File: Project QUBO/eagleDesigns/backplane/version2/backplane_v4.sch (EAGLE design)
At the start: 206 parts, among them IC1 MC78M08ABDTG, U1 TUSB2077ALQFP

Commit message: 
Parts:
- removed C12, C14, C15: 100n, resistor:C-USC0805
- removed C13: 4.7u, resistor:C-USC0805
- removed C21, C22, C23, C24, C25: (no value), resistor:C-USC0805
- removed IC1: MC78M08ABDTG, linear:MC78M08ABDTG
- removed IMU_FTDI: FT232RQ, ftdichip:FT232RQ
- removed IMU_TTL-TO-RS422: AD7306JRZ, analog_devices:AD7306JRZ
- removed LED5, LED6: (no value), led:LEDCHIPLED_0805
- added 2PIN_4: Magnetic Reed Switch plug, molex:KK254_VERT_2PIN22-29-2021
- added D1: Vz=14V, diode:ZENER-DIODESOD123
- added R62, R63: 5k, resistor:R-US_R0805
- added U$42, U$52, U$53, U$54, U$55, U$56, U$57, U$58, U$59, U$60, U$61, U$62, U$63: PRTR5V0U2X, NXP:PRTR5V0U2X
- added U$43: AHRS USB header, connectors:USB_4PIN_VERT
- added U$44, U$48: (no value), littelfuse:V5.5MLA0805
- added U$45, U$49, U$51: 100u_tant, avx:F93-XX-XXX-X-A
- added U$46: I2C level shifter, texas:PCA9306DCT
- added U$47: Depth Sensor header, connectors:DF13-4
- added U$50: P82B715, NXP:P82B715
- R1: value 120 -> 200k
- R61: value 15k -> 50k
- R8, R9: value 270 -> 5k
- U$10: value (none) -> IMU USB header; device hirose:HR30-6R-6PD -> connectors:USB_4PIN_VERT
- U$11: value 1U_tant -> (none); device avx:F93-XX-XXX-X-A -> littelfuse:V5.5MLA0805
- U$12: value 1U_tant -> 100u_tant
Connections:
- removed net 8V: IC1.VO, U$10.2, U$12.+
- removed net IMU_RX: IMU_FTDI.RXD, IMU_TTL-TO-RS422.R1-OUT
- removed net IMU_RXD_M: IMU_TTL-TO-RS422.R1-IN(B), R1.1, U$10.4, U$9.I/O_2
- removed net IMU_RXD_P: IMU_TTL-TO-RS422.R1-IN/(A), R1.2, U$10.3, U$9.I/O_1
- removed net N$26: C12.1, IMU_FTDI.3V3OUT
- removed net N$27: IMU_FTDI.CBUS1, LED6.C
- removed net N$28: IMU_FTDI.CBUS0, LED5.C
- removed net N$29: LED5.A, R8.1
- removed net N$30: LED6.A, R9.1
- removed net N$37: C21.1, IMU_TTL-TO-RS422.V+
- removed net N$38: C22.1, IMU_TTL-TO-RS422.V-
- removed net N$40: C23.2, IMU_TTL-TO-RS422.C1-
- removed net N$41: C24.1, IMU_TTL-TO-RS422.C2+
- removed net N$42: C24.2, IMU_TTL-TO-RS422.C2-
- new net DEPTH_SCL: R62.2, U$46.SCL1, U$47.2
- new net DEPTH_SDA: R63.2, U$46.SDA1, U$47.3
- new net GND1: U$11.P$1, U$12.-
- new net GND2: U$44.P$1, U$45.-
- new net GND3: U$48.P$1, U$49.-
- new net SCL_1_UNBUF: R8.2, U$46.SCL2, U$50.SX
- new net SDA_1_UNBUF: R9.2, U$46.SDA2, U$50.SY
- new net USB_5_5V1: U$11.P$2, U$12.+
- new net USB_5_5V2: U$44.P$2, U$45.+
- new net USB_5_5V3: U$48.P$2, U$49.+
- net 12V: now also 2PIN_4.P$1, U$42.VCC; no longer IC1.VI, U$11.+
- net 3V3: now also R62.1, R63.1, U$46.VREF1
- net 5V: now also R1.2, R8.1, R9.1, U$10.1, U$43.1, U$47.1, U$50.VCC, U$52.VCC, U$53.VCC, U$54.VCC, U$55.VCC, U$56.VCC, U$57.VCC, U$58.VCC, U$59.VCC, U$60.VCC, U$61.VCC, U$62.VCC, U$63.VCC; no longer C13.1, C14.1, C15.1, C25.1, IMU_FTDI.!RESET, IMU_FTDI.VCC, IMU_FTDI.VCCIO, IMU_TTL-TO-RS422.VCC, R8.2, R9.2
- net ACT-PWR_PRE-KILL: now also D1.C
- net AHRS_USB_M: now also U$42.I/O_2, U$43.3
- net AHRS_USB_P: now also U$42.I/O_1, U$43.2
- net BATT1_SCL: now also U$62.I/O_1
- net BATT1_SDA: now also U$62.I/O_2
- net BATT2_SCL: now also U$61.I/O_1
- net BATT2_SDA: now also U$61.I/O_2
- net CANH: now also U$53.I/O_2
- net CANL: now also U$53.I/O_1
- net CTS_5: now also U$55.I/O_2
- net DVL_HCTS: now also U$58.I/O_2
- net DVL_HRTS: now also U$57.I/O_1
- net DVL_HRX: now also U$56.I/O_2
- net DVL_HTX: now also U$57.I/O_2
- net DVL_SCTS: now also U$56.I/O_1
- net DVL_SRTS: now also U$59.I/O_2
- net DVL_SRX: now also U$58.I/O_1
- net DVL_STX: now also U$59.I/O_1
- net GND: now also U$10.4, U$42.GND, U$43.4, U$46.GND, U$47.4, U$50.GND, U$51.-, U$52.GND, U$53.GND, U$54.GND, U$55.GND, U$56.GND, U$57.GND, U$58.GND, U$59.GND, U$60.GND, U$61.GND, U$62.GND, U$63.GND; no longer C12.2, C13.2, C14.2, C15.2, C21.2, C22.2, C25.2, IC1.GND, IMU_FTDI.GND, IMU_FTDI.GND@1, IMU_FTDI.GND@2, IMU_FTDI.GND@A, IMU_FTDI.TEST, IMU_TTL-TO-RS422.232/!422!, IMU_TTL-TO-RS422.GND@14, IMU_TTL-TO-RS422.GND@18, U$10.5, U$11.-, U$12.-
- net IMU_USB_M: now also U$10.3, U$9.I/O_2; no longer IMU_FTDI.USBDM
- net IMU_USB_P: now also U$10.2, U$9.I/O_1; no longer IMU_FTDI.USBDP
- net N$39: now also R1.1, U$46.EN, U$46.VREF2, U$51.+; no longer C23.1, IMU_TTL-TO-RS422.C1+
- net N$73: now also 2PIN_4.P$2, D1.A
- net RTS_5: now also U$55.I/O_1
- net RX_5: now also U$54.I/O_1
- net SCL_1: now also U$50.LX
- net SCL_2: now also U$63.I/O_1
- net SCL_3: now also U$52.I/O_1
- net SDA_1: now also U$50.LY
- net SDA_2: now also U$63.I/O_2
- net SDA_3: now also U$52.I/O_2
- net SHORE_SCL: now also U$60.I/O_1
- net SHORE_SDA: now also U$60.I/O_2
- net TX_5: now also U$54.I/O_2
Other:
- note added: "AHRS Connection"
- note added: "DVL USB-UART Converters"
- note added: "Depth Sensor Connection"
- note removed: "USB-UART Converters"
- moved on the sheet: R1, R8, R9, U$12

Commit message: 
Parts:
- added D10, D11, D12, D13, D14, D15, D16, D17, D18, D19, D2, D20, D21, D22, D23, D24, D25, D26, D27, D28, D29, D3, D30, D31, D32, D33, D34, D35, D4, D5, D6, D7, D8, D9: (no value), diode:ZENER-DIODESOD123
- added U$64, U$65, U$66, U$67, U$70, U$71, U$72, U$73, U$74, U$75, U$76, U$77, U$78, U$79, U$80, U$81, U$82, U$83, U$84, U$85, U$86, U$87, U$88, U$89, U$90, U$91, U$92, U$93, U$94, U$95, U$96, U$97, U$98, U$99: 0.1u, avx:F93-XX-XXX-X-A
- added U$68: (no value), littelfuse:V5.5MLA0805
- added U$69: 100u_tant, avx:F93-XX-XXX-X-A
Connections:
- removed net N$73: 2PIN_4.P$2, D1.A, R61.1, U$41.P$3
- new net KILL-SWT-GATE: 2PIN_4.P$2, D1.A, D10.C, R61.1, U$41.P$3, U$74.+
- net 12V: now also D11.C, D15.C, D19.C, D23.C, D27.C, D4.C, D5.C, D6.C, D7.C, U$64.+, U$65.+, U$66.+, U$67.+, U$75.+, U$79.+, U$83.+, U$87.+, U$91.+
- net 3V3: now also D13.C, D17.C, D21.C, D25.C, U$77.+, U$81.+, U$85.+, U$89.+
- net 5V: now also D12.C, D16.C, D2.C, D20.C, D24.C, D3.C, U$68.P$2, U$69.+, U$70.+, U$71.+, U$76.+, U$80.+, U$84.+, U$88.+
- net ACT-PWR_POST-KILL: now also D8.C, U$72.+
- net ACT-PWR_PRE-KILL: now also D9.C, U$73.+
- net GND: now also D10.A, D11.A, D12.A, D13.A, D14.A, D15.A, D16.A, D17.A, D18.A, D19.A, D2.A, D20.A, D21.A, D22.A, D23.A, D24.A, D25.A, D26.A, D27.A, D28.A, D29.A, D3.A, D30.A, D31.A, D32.A, D33.A, D34.A, D35.A, D4.A, D5.A, D6.A, D7.A, D8.A, D9.A, U$64.-, U$65.-, U$66.-, U$67.-, U$68.P$1, U$69.-, U$70.-, U$71.-, U$72.-, U$73.-, U$74.-, U$75.-, U$76.-, U$77.-, U$78.-, U$79.-, U$80.-, U$81.-, U$82.-, U$83.-, U$84.-, U$85.-, U$86.-, U$87.-, U$88.-, U$89.-, U$90.-, U$91.-, U$92.-, U$93.-, U$94.-, U$95.-, U$96.-, U$97.-, U$98.-, U$99.-
- net V_BATT: now also D14.C, D18.C, D22.C, D26.C, D28.C, D29.C, D30.C, D31.C, D32.C, D33.C, D34.C, D35.C, U$78.+, U$82.+, U$86.+, U$90.+, U$92.+, U$93.+, U$94.+, U$95.+, U$96.+, U$97.+, U$98.+, U$99.+
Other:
- note added: "Power Line Protections"
- moved on the sheet: SYS-GND_0, SYS-GND_1, SYS-GND_2, SYS-GND_3

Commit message: 
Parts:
- removed SYS-GND_0, SYS-GND_1, SYS-GND_2, SYS-GND_3: SUPERSABRE_2CIRCUIT, molex:SUPERSABRE_2CIRCUIT
- removed U$17: (no value), connectors:USB_4PIN_VERT
- removed U$21: PRTR5V0U2X, NXP:PRTR5V0U2X
- removed U$26: (no value), littelfuse:V5.5MLA0805
- removed U$36: 100u_tant, avx:F93-XX-XXX-X-A
- removed U$74: 0.1u, avx:F93-XX-XXX-X-A
- added D36, D37, D39, D40, D41: 5V, diode:ZENER-DIODESOD123
- added R64, R65, R66: 15k, resistor:R-US_R0805
- added U$100: SYSTEM GROUND, molex:SUPERSABRE_8CIRCUIT
- C26: value 0.1u\ -> 0.1u
- C27, C29: value (none) -> 0.1u
- D1: value Vz=14V -> 14V
- D10, D12, D16, D2, D20, D24, D3: value (none) -> 5V
- D11, D15, D19, D23, D27, D4, D5, D6, D7: value (none) -> 12V
- D13, D17, D21, D25: value (none) -> 3V3
- D14, D18, D22, D26, D28, D29, D30, D31, D32, D33, D34, D35, D8, D9: value (none) -> V_BATT
- LED1, LED3: value (none) -> Red
- LED2, LED4, LED7: value (none) -> Green
- U$64, U$65, U$66, U$67, U$70, U$71, U$72, U$73, U$75, U$76, U$77, U$78, U$79, U$80, U$81, U$82, U$83, U$84, U$85, U$86, U$87, U$88, U$89, U$90, U$91, U$92, U$93, U$94, U$95, U$96, U$97, U$98, U$99: value 0.1u -> 0.1u_tant
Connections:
- net !USB_7_PWR! renamed !EXT_USB_PWR!
- removed net !USB_7_OVERCUR!: G1.!OC3!, U1.!OVERCUR7!
- removed net USB_7_5V: G1.OUT3, U$17.1, U$26.P$2, U$36.+
- removed net USB_7_M: R34.2, R47.1, U$17.3, U$21.I/O_2
- removed net USB_7_P: R35.2, R48.1, U$17.2, U$21.I/O_1
- new net !EXT_USB_OVERCUR!: G1.!OC3!, R66.1, U1.!OVERCUR7!
- new net EXT_USB_5V: 5.7.P$4, D41.C, G1.OUT3, U$68.P$2, U$69.+
- net !USB_5_OVERCUR!: now also R64.2
- net !USB_6_OVERCUR!: now also R65.1
- net 3V3: now also R64.1, R65.2, R66.2
- net 5V: no longer 5.7.P$4, U$21.VCC, U$68.P$2, U$69.+
- net EXT_USB_M: now also R34.2, R47.1
- net EXT_USB_P: now also R35.2, R48.1
- net GND: now also D39.A, D40.A, D41.A, U$100.1, U$100.2, U$100.3, U$100.4, U$100.5, U$100.6, U$100.7, U$100.8; no longer D10.A, SYS-GND_0.P$1, SYS-GND_0.P$2, SYS-GND_1.P$1, SYS-GND_1.P$2, SYS-GND_2.P$1, SYS-GND_2.P$2, SYS-GND_3.P$1, SYS-GND_3.P$2, U$17.4, U$21.GND, U$26.P$1, U$36.-, U$74.-
- net GND1: now also D37.A
- net GND2: now also D36.A
- net GND3: now also D10.A
- net KILL-SWT-GATE: no longer D10.C, U$74.+
- net USB_5_5V: now also D40.C
- net USB_5_5V1: now also D37.C
- net USB_5_5V2: now also D36.C
- net USB_5_5V3: now also D10.C
- net USB_6_5V: now also D39.C
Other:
- moved on the sheet: D10

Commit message: 
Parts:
- G1: value (none) -> TPS2044BBD-SOIC
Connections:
- net 12V: no longer U$42.VCC, U$9.VCC
- net 5V: now also U$42.VCC, U$9.VCC
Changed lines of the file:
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@@
 <text x="-284.48" y="-396.24" size="6.4516" layer="91">IMU Connection</text>
 <text x="-561.34" y="-144.78" size="6.4516" layer="91">Debug LED SPI</text>
-<text x="-530.86" y="-342.9" size="6.4516" layer="91">GPIO USBs</text>
+<text x="-533.4" y="-302.26" size="6.4516" layer="91">GPIO USBs</text>
 <text x="-472.44" y="203.2" size="6.4516" layer="91">7-port USB hub</text>
 <text x="-297.18" y="-142.24" size="6.4516" layer="91">2-port USB hub (DVL)</text>
@@
 <pinref part="D24" gate="G$1" pin="C"/>
 </segment>
+<segment>
+<pinref part="U$9" gate="G$1" pin="VCC"/>
+<wire x1="-266.7" y1="-370.84" x2="-259.08" y2="-370.84" width="0.1524" layer="91"/>
+<label x="-264.16" y="-370.84" size="1.778" layer="95"/>
+</segment>
+<segment>
+<pinref part="U$42" gate="G$1" pin="VCC"/>
+<wire x1="-269.24" y1="-434.34" x2="-261.62" y2="-434.34" width="0.1524" layer="91"/>
+<label x="-266.7" y="-434.34" size="1.778" layer="95"/>
+</segment>
 </net>
 <net name="12V" class="0">
@@
 </segment>
 <segment>
-<pinref part="U$9" gate="G$1" pin="VCC"/>
-<wire x1="-266.7" y1="-370.84" x2="-259.08" y2="-370.84" width="0.1524" layer="91"/>
-<label x="-264.16" y="-370.84" size="1.778" layer="95"/>
-</segment>
-<segment>
-<pinref part="U$42" gate="G$1" pin="VCC"/>
-<wire x1="-269.24" y1="-434.34" x2="-261.62" y2="-434.34" width="0.1524" layer="91"/>
-<label x="-266.7" y="-434.34" size="1.778" layer="95"/>
-</segment>
-<segment>
 <pinref part="2PIN_4" gate="U1" pin="P$1"/>
 <wire x1="398.78" y1="0" x2="393.7" y2="0" width="0.1524" layer="91"/>
@@
 <segment>
 <wire x1="-576.58" y1="-215.9" x2="-439.42" y2="-215.9" width="0.1524" layer="91"/>
-<wire x1="-439.42" y1="-215.9" x2="-439.42" y2="-353.06" width="0.1524" layer="91"/>
-<wire x1="-439.42" y1="-353.06" x2="-576.58" y2="-353.06" width="0.1524" layer="91"/>
-<wire x1="-576.58" y1="-353.06" x2="-576.58" y2="-215.9" width="0.1524" layer="91"/>
+<wire x1="-439.42" y1="-215.9" x2="-439.42" y2="-312.42" width="0.1524" layer="91"/>
+<wire x1="-439.42" y1="-312.42" x2="-576.58" y2="-312.42" width="0.1524" layer="91"/>
+<wire x1="-576.58" y1="-312.42" x2="-576.58" y2="-215.9" width="0.1524" layer="91"/>
 </segment>
 </net>

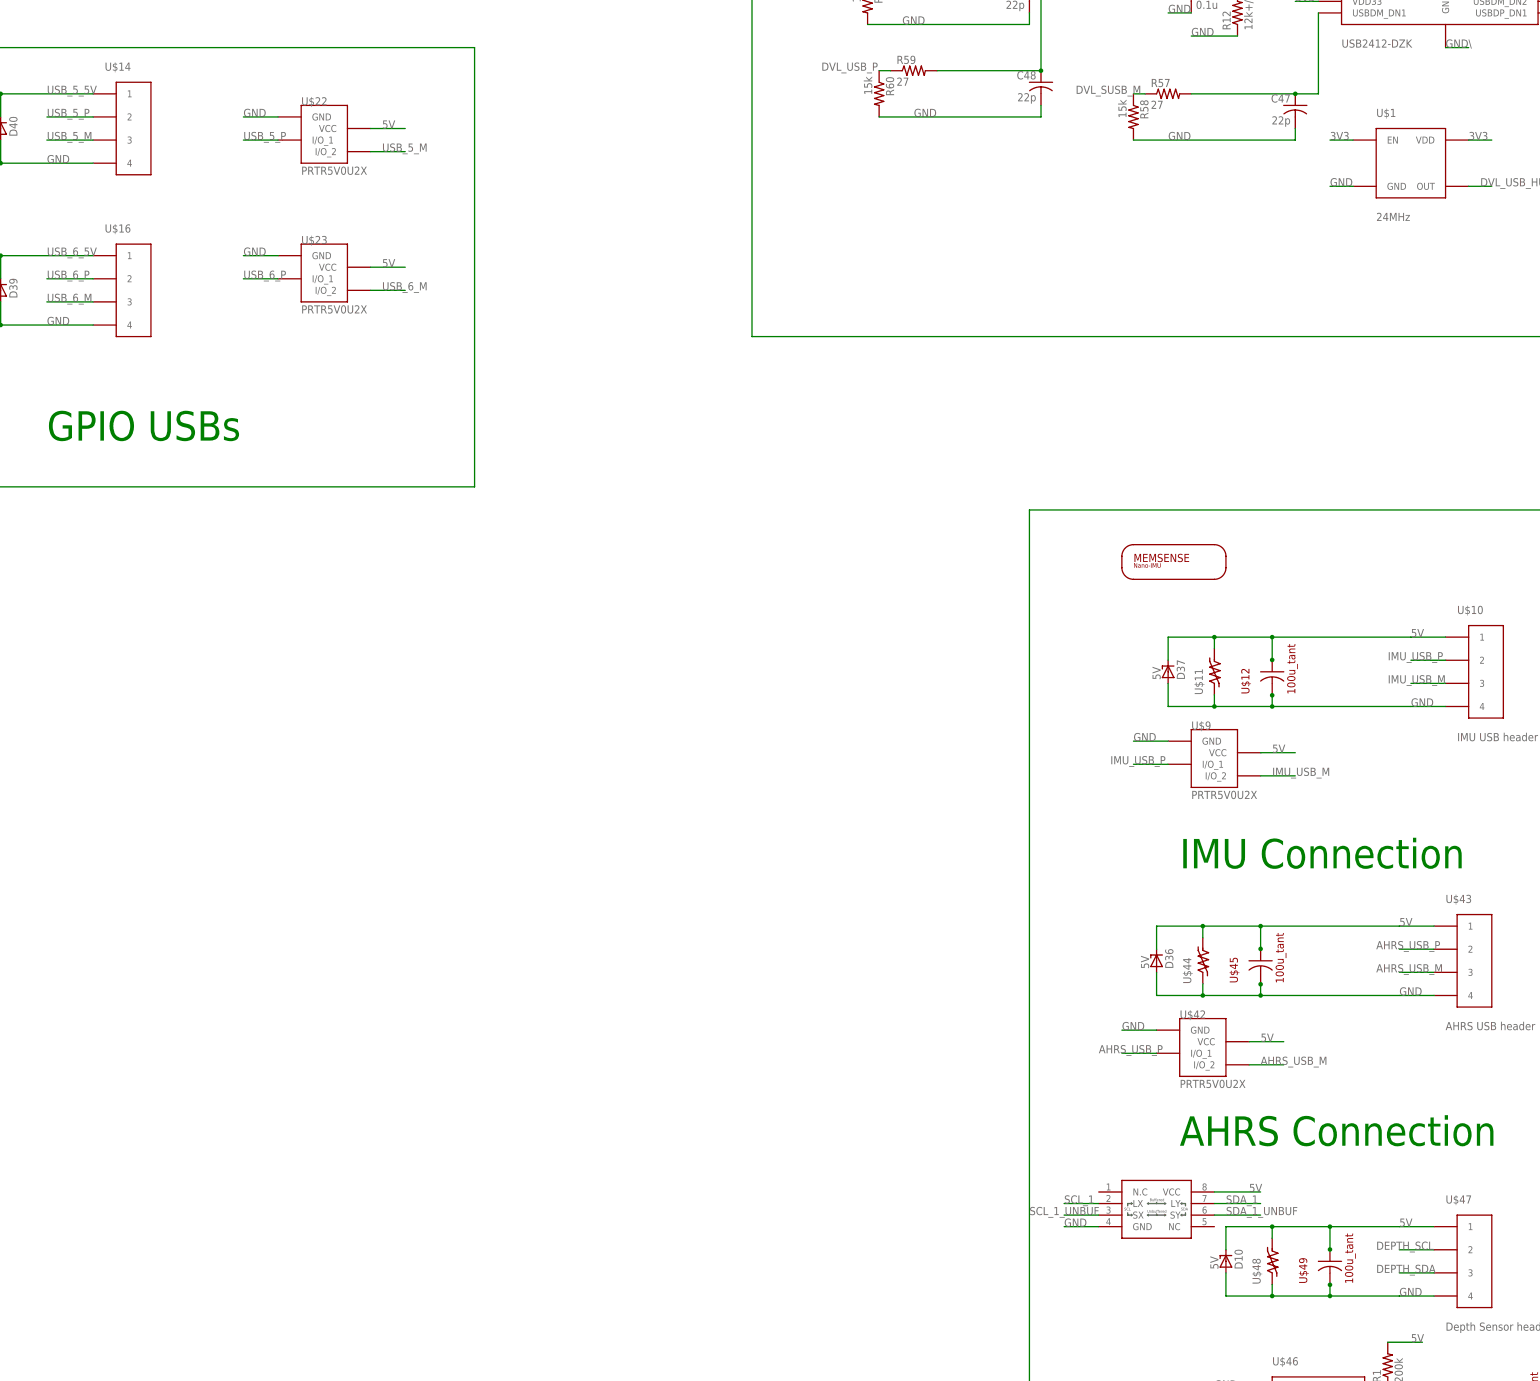
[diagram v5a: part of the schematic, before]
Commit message: 
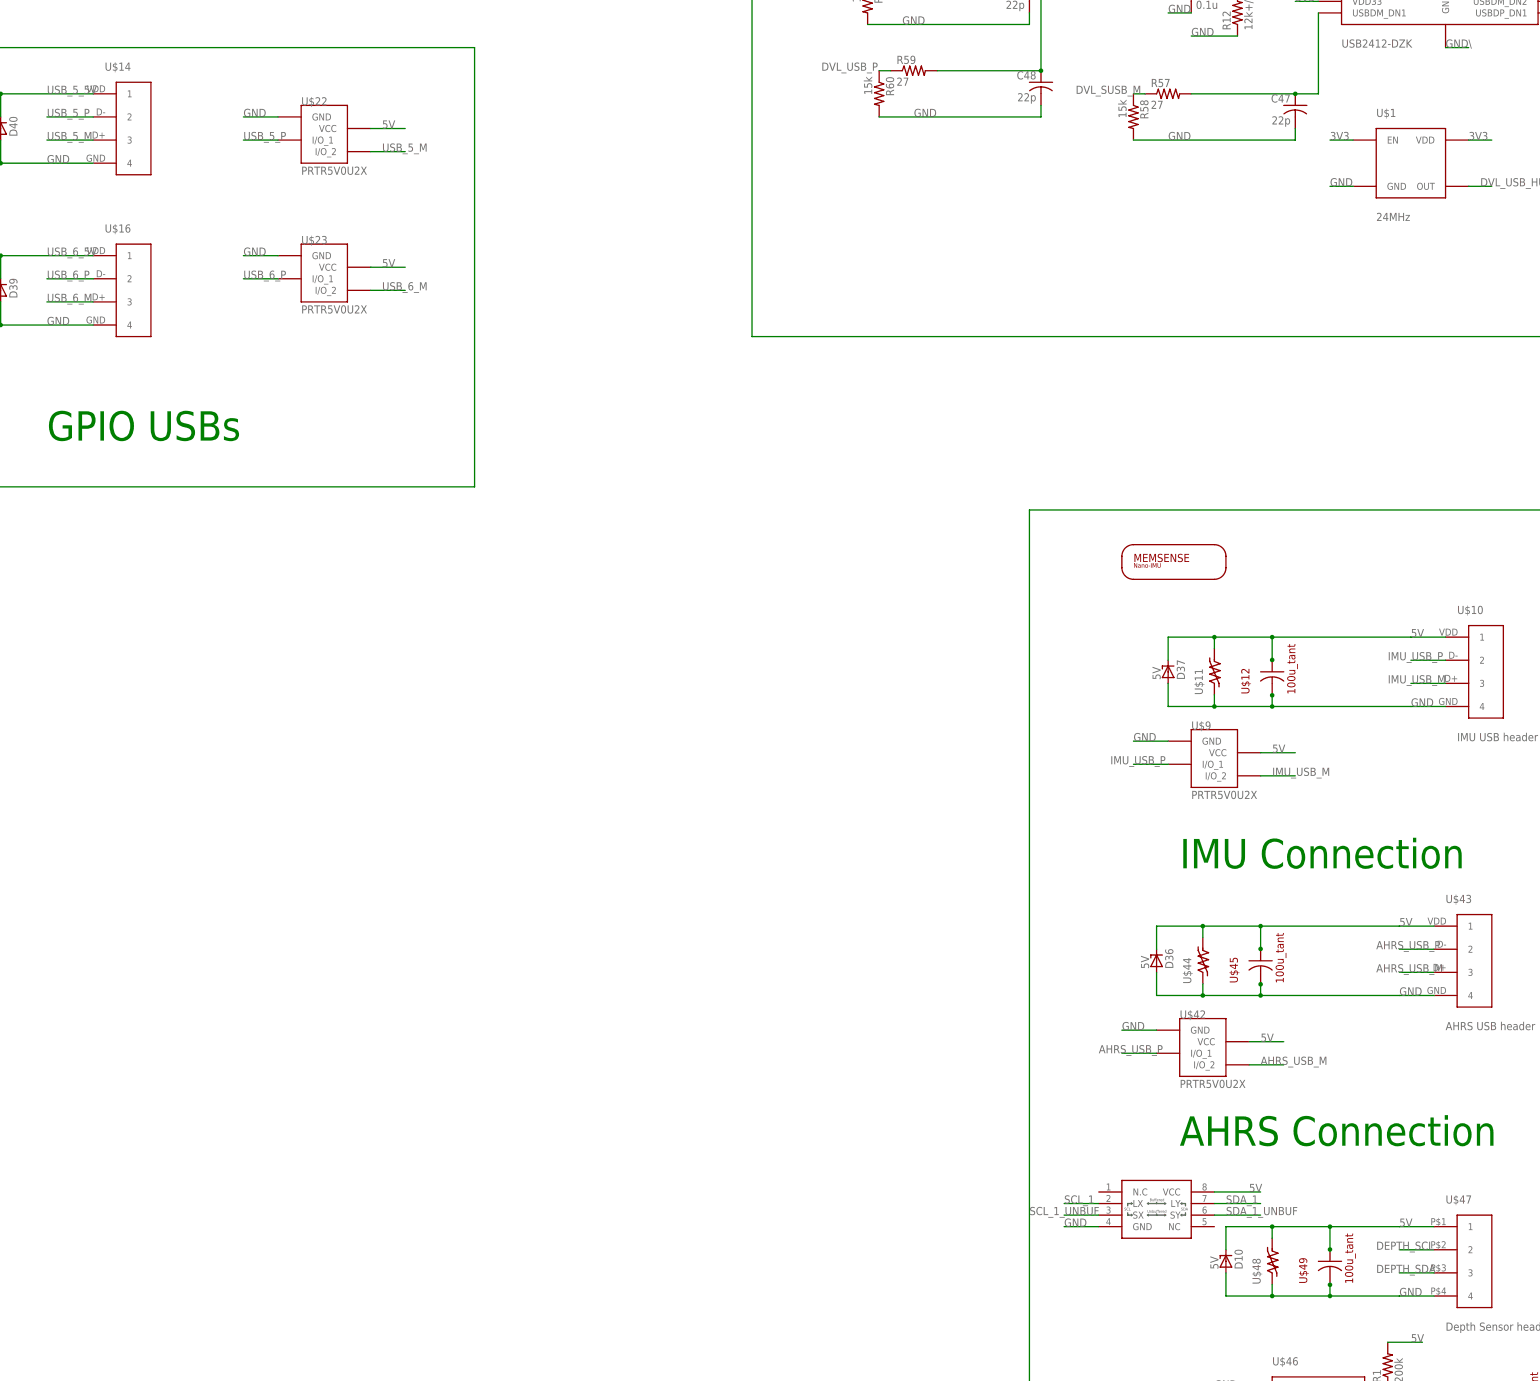
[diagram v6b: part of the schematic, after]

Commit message: 
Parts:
- added U$101, U$102, U$103, U$104, U$105, U$106, U$107, U$108, U$109, U$17, U$21, U$26, U$36, U$74: (no value), resistor:FERRITE_BEAD
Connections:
- removed net GND1: D37.A, U$11.P$1, U$12.-
- removed net GND2: D36.A, U$44.P$1, U$45.-
- removed net GND3: D10.A, U$48.P$1, U$49.-
- removed net USB_5_5V1: D37.C, U$11.P$2, U$12.+
- removed net USB_5_5V2: D36.C, U$44.P$2, U$45.+
- removed net USB_5_5V3: D10.C, U$48.P$2, U$49.+
- new net N$27: U$10.1, U$17.P$2
- new net N$28: U$10.4, U$21.P$2
- new net N$29: U$10.SHIELD, U$26.P$2
- new net N$30: U$108.P$2, U$47.1
- new net N$37: U$109.P$2, U$47.4
- new net N$38: U$43.1, U$74.P$2
- new net N$40: U$101.P$2, U$43.4
- new net N$41: U$36.P$2, U$43.SHIELD
- new net N$42: U$107.P$2, U$14.1
- new net N$73: U$106.P$2, U$14.4
- new net N$80: U$105.P$2, U$14.SHIELD
- new net N$83: U$104.P$2, U$16.SHIELD
- new net N$84: U$102.P$2, U$16.1
- new net N$85: U$103.P$2, U$16.4
- net 5V: now also D10.C, D36.C, D37.C, U$108.P$1, U$11.P$2, U$12.+, U$17.P$1, U$44.P$2, U$45.+, U$48.P$2, U$49.+, U$74.P$1; no longer U$10.1, U$43.1, U$47.1
- net GND: now also D10.A, D36.A, D37.A, U$101.P$1, U$103.P$1, U$104.P$1, U$105.P$1, U$106.P$1, U$109.P$1, U$11.P$1, U$12.-, U$21.P$1, U$26.P$1, U$36.P$1, U$44.P$1, U$45.-, U$48.P$1, U$49.-; no longer U$10.4, U$14.4, U$16.4, U$43.4, U$47.4
- net USB_5_5V: now also U$107.P$1; no longer U$14.1
- net USB_6_5V: now also U$102.P$1; no longer U$16.1
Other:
- moved on the sheet: U$47
